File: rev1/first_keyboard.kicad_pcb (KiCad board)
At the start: 2 copper layers, 80 parts, among them SW1 SW_Push, SW10 SW_Push, SW11 SW_Push, SW12 SW_Push, SW13 SW_Push, SW14 SW_Push, SW15 SW_Push, SW16 SW_Push, SW17 SW_Push, SW18 SW_Push, SW19 SW_Push, SW2 SW_Push, SW20 SW_Push, SW21 SW_Push, SW22 SW_Push, SW23 SW_Push, SW24 SW_Push, SW25 SW_Push, SW26 SW_Push, SW27 SW_Push, SW28 SW_Push, SW29 SW_Push, SW3 SW_Push, SW30 SW_Push, SW31 SW_Push, SW32 SW_Push, SW33 SW_Push, SW34 SW_Push, SW35 SW_Push, SW36 SW_Push, SW37 SW_Push, SW38 SW_Push, SW39 SW_Push, SW4 SW_Push, SW40 SW_Push, SW5 SW_Push, SW6 SW_Push, SW7 SW_Push, SW8 SW_Push, SW9 SW_Push, U1 Pico

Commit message: feat:ダイオードの番号降り直しと整列\
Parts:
- SW1: footprint kbd_Parts:ResetSW -> kbd_SW:CherryMX_Hotswap_1u
- SW39: footprint kbd_SW:CherryMX_Hotswap_1u -> kbd_SW:CherryMX_Hotswap_2u
- SW40: footprint kbd_SW:CherryMX_Hotswap_2u -> kbd_Parts:ResetSW
- moved SW1 312.8 mm to (23.8, 45.2)
- moved U1 178.0 mm to (147.7, 61.9)
- moved SW9 134.8 mm to (61.9, 45.2)
- moved SW17 119.1 mm to (100.0, 45.2)
- moved SW40 118.2 mm to (381.0, 132.5)
- moved SW12 114.4 mm to (176.2, 102.4)
- moved SW16 114.4 mm to (195.3, 102.4)
- moved SW5 91.5 mm to (42.9, 45.2)
- moved SW13 81.0 mm to (81.0, 45.2)
- moved SW23 77.5 mm to (176.2, 45.2)
- moved SW4 76.3 mm to (100.0, 102.4)
- moved SW8 76.3 mm to (119.1, 102.4)
- moved SW20 55.7 mm to (119.1, 45.2)
- moved SW29 55.7 mm to (214.3, 45.2)
- moved SW32 55.7 mm to (233.4, 45.2)
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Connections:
- SW1 pad 1: reset -> Col0
- SW1 pad 2: GND -> Net-(D1-A)
- SW10 pad 2: Net-(D9-A) -> Net-(D10-A)
- SW11 pad 2: Net-(D10-A) -> Net-(D11-A)
- SW12 pad 2: Net-(D11-A) -> Net-(D12-A)
- SW13 pad 1: Col2 -> Col3
- SW13 pad 2: Net-(D12-A) -> Net-(D13-A)
- SW14 pad 2: Net-(D13-A) -> Net-(D14-A)
- SW15 pad 2: Net-(D14-A) -> Net-(D15-A)
- SW16 pad 2: Net-(D15-A) -> Net-(D16-A)
- SW17 pad 1: Col3 -> Col4
- SW17 pad 2: Net-(D16-A) -> Net-(D17-A)
- SW18 pad 2: Net-(D17-A) -> Net-(D18-A)
- SW19 pad 2: Net-(D18-A) -> Net-(D19-A)
- SW2 pad 2: Net-(D1-A) -> Net-(D2-A)
- SW20 pad 1: Col4 -> Col5
- SW20 pad 2: Net-(D19-A) -> Net-(D20-A)
- SW21 pad 2: Net-(D20-A) -> Net-(D21-A)
- SW22 pad 2: Net-(D21-A) -> Net-(D22-A)
- SW23 pad 1: Col5 -> Col6
- SW23 pad 2: Net-(D22-A) -> Net-(D23-A)
- SW24 pad 2: Net-(D23-A) -> Net-(D24-A)
- SW25 pad 2: Net-(D24-A) -> Net-(D25-A)
- SW26 pad 1: Col6 -> Col7
- SW26 pad 2: Net-(D25-A) -> Net-(D26-A)
- SW27 pad 2: Net-(D26-A) -> Net-(D27-A)
- SW28 pad 2: Net-(D27-A) -> Net-(D28-A)
- SW29 pad 1: Col7 -> Col8
- SW29 pad 2: Net-(D28-A) -> Net-(D29-A)
- SW3 pad 2: Net-(D2-A) -> Net-(D3-A)
- SW30 pad 2: Net-(D29-A) -> Net-(D30-A)
- SW31 pad 2: Net-(D30-A) -> Net-(D31-A)
- SW32 pad 1: Col8 -> Col9
- SW32 pad 2: Net-(D31-A) -> Net-(D32-A)
- SW33 pad 2: Net-(D32-A) -> Net-(D33-A)
- SW34 pad 2: Net-(D33-A) -> Net-(D34-A)
- SW35 pad 1: Col9 -> Col10
- SW35 pad 2: Net-(D34-A) -> Net-(D35-A)
- SW36 pad 2: Net-(D35-A) -> Net-(D36-A)
- SW37 pad 2: Net-(D36-A) -> Net-(D37-A)
- SW38 pad 1: Col10 -> Col11
- SW38 pad 2: Net-(D37-A) -> Net-(D38-A)
- SW39 pad 2: Net-(D38-A) -> Net-(D39-A)
- SW4 pad 2: Net-(D3-A) -> Net-(D4-A)
- SW40 pad 1: Col11 -> reset
- SW40 pad 2: Net-(D39-A) -> GND
- SW5 pad 1: Col0 -> Col1
- SW5 pad 2: Net-(D4-A) -> Net-(D5-A)
- SW6 pad 2: Net-(D5-A) -> Net-(D6-A)
- SW7 pad 2: Net-(D6-A) -> Net-(D7-A)
- SW8 pad 2: Net-(D7-A) -> Net-(D8-A)
- SW9 pad 1: Col1 -> Col2
- SW9 pad 2: Net-(D8-A) -> Net-(D9-A)

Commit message: feat: すべて整列済み\
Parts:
- moved D1 291.8 mm to (33.3, 51.0), turned to 90 degrees
- moved D2 288.8 mm to (33.3, 70.0), turned to 90 degrees
- moved D3 286.8 mm to (33.3, 89.1), turned to 90 degrees
- moved D5 275.8 mm to (52.4, 51.0), turned to 90 degrees
- moved D6 272.0 mm to (52.4, 70.0), turned to 90 degrees
- moved D7 269.1 mm to (52.4, 89.1), turned to 90 degrees
- moved D9 260.6 mm to (71.4, 51.0), turned to 90 degrees
- moved D10 255.9 mm to (71.4, 70.0), turned to 90 degrees
- moved D11 252.2 mm to (71.4, 89.1), turned to 90 degrees
- moved D13 246.4 mm to (90.5, 51.0), turned to 90 degrees
- moved D14 240.7 mm to (90.5, 70.0), turned to 90 degrees
- moved D15 239.3 mm to (90.5, 89.1), turned to 90 degrees
- moved SW40 235.0 mm to (147.6, 104.8), turned to 180 degrees
- moved D17 229.0 mm to (109.5, 51.0), turned to 90 degrees
- moved D18 224.8 mm to (109.5, 70.0), turned to 90 degrees
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
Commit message: feat: ダイオードそろえた
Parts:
- moved D8 76.8 mm to (52.4, 98.2)
- moved D20 70.6 mm to (76.2, 98.2)
- moved D4 67.4 mm to (42.9, 98.2)
- moved D17 62.2 mm to (69.1, 98.2)
- moved D23 59.3 mm to (221.5, 98.2)
- moved D21 57.4 mm to (78.6, 98.2)
- moved D13 54.0 mm to (64.3, 98.2)
- moved D26 52.9 mm to (228.6, 98.2)
- moved D38 52.9 mm to (257.2, 98.2)
- moved D9 50.1 mm to (54.8, 98.2)
- moved D29 48.8 mm to (235.7, 98.2)
- moved D35 48.8 mm to (250.0, 98.2)
- moved D22 48.5 mm to (81.0, 98.2)
- moved D5 47.8 mm to (45.2, 98.2)
- moved D18 47.4 mm to (71.4, 98.2)
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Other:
- board outline added: 271.5 x 85.7 mm

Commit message: feat: m3spacer
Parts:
- added Ref**: Val**, kbd_Hole:m3_Spacer_Hole, F.Cu at (274.3, 32.0)
- added Ref**: Val**, kbd_Hole:m3_Spacer_Hole, F.Cu at (159.7, 111.5)
- added Ref**: Val**, kbd_Hole:m3_Spacer_Hole, F.Cu at (274.3, 97.0)
- added Ref**: Val**, kbd_Hole:m3_Spacer_Hole, F.Cu at (135.6, 111.5)
- added Ref**: Val**, kbd_Hole:m3_Spacer_Hole, F.Cu at (120.7, 32.0)
- added Ref**: Val**, kbd_Hole:m3_Spacer_Hole, F.Cu at (171.4, 32.0)
- added Ref**: Val**, kbd_Hole:m3_Spacer_Hole, F.Cu at (20.3, 97.0)
- added Ref**: Val**, kbd_Hole:m3_Spacer_Hole, F.Cu at (20.3, 32.0)
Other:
- board size 271.5 x 85.7 mm -> 271.5 x 88.6 mm

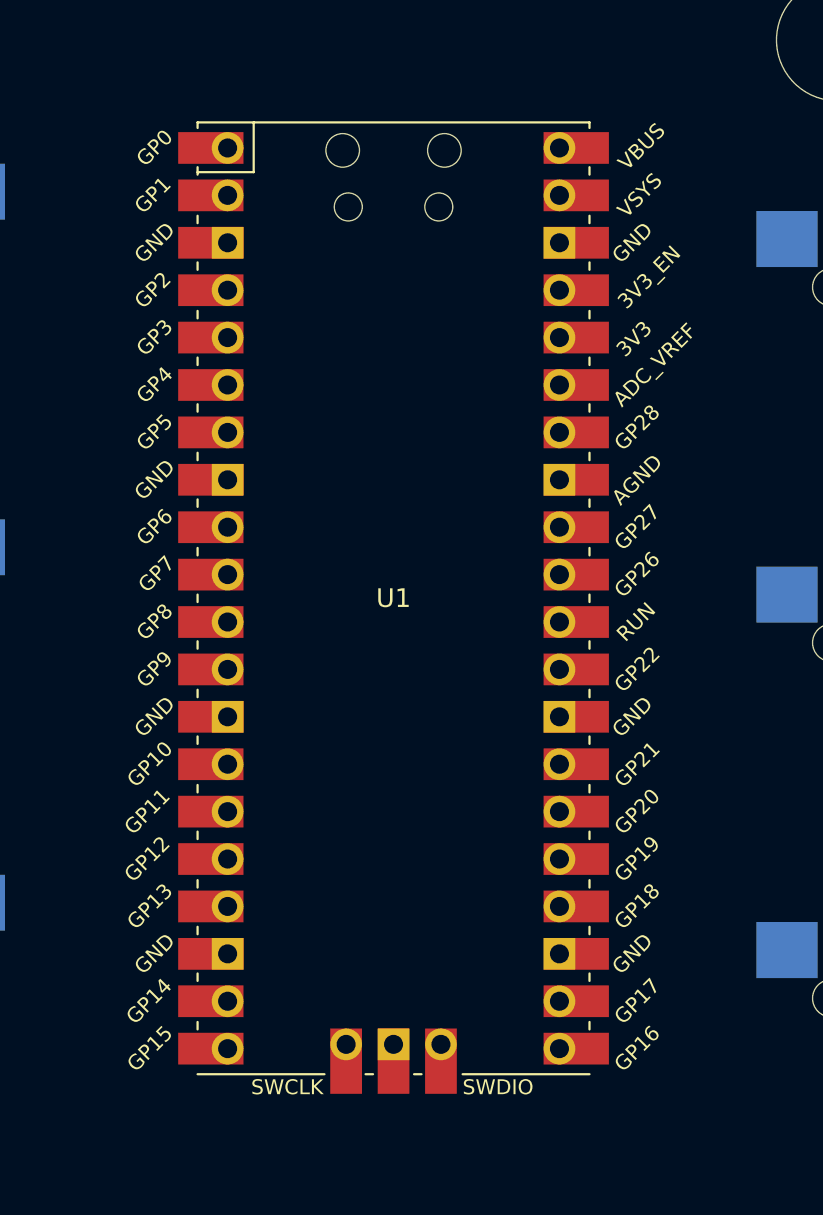
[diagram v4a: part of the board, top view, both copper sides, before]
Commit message: feat: picoを裏面に
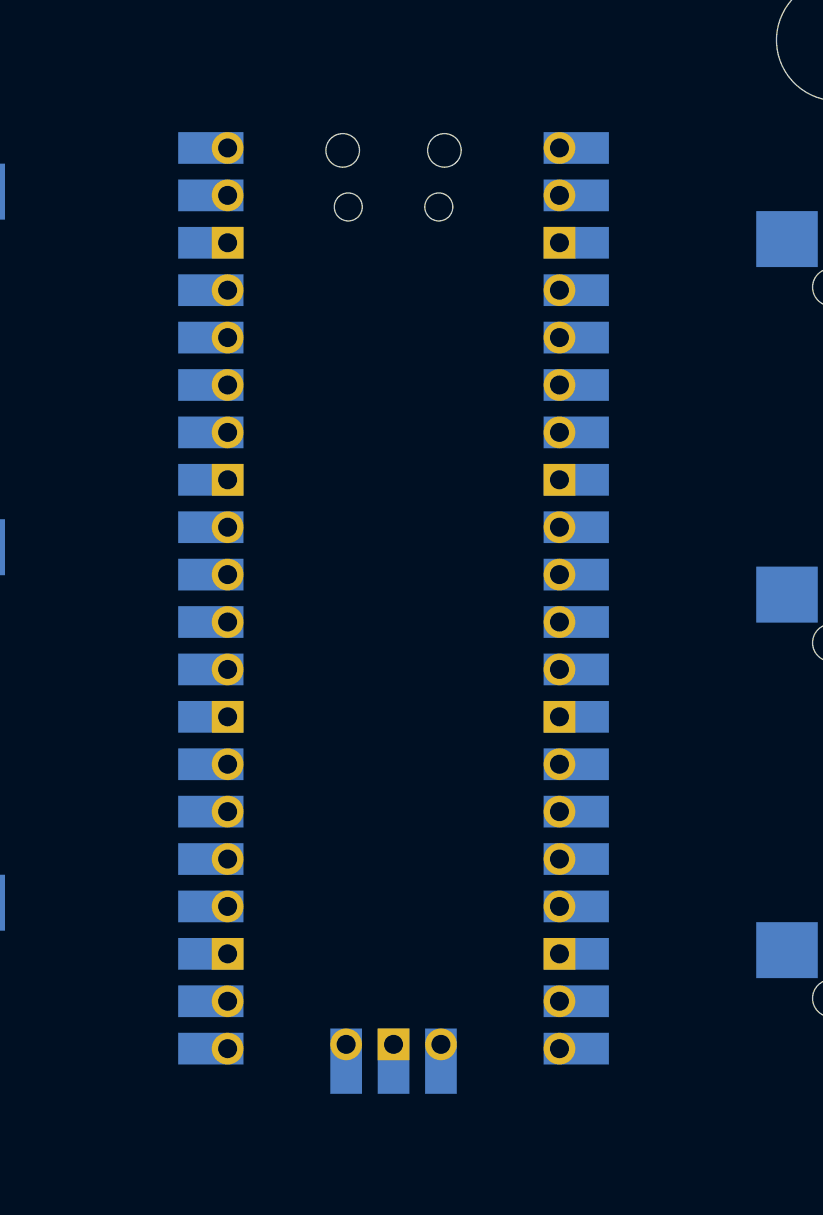
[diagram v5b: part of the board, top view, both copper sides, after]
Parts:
- U1: moved to B.Cu
- turned U1 to 180 degrees

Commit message: feat: ダイオードをスイッチの近くに大移動
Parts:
- Ref1: renamed from Ref**; value Val** -> Val1
- Ref2: renamed from Ref**; value Val** -> Val2
- Ref3: renamed from Ref**; value Val** -> Val3
- Ref4: renamed from Ref**; value Val** -> Val4
- Ref5: renamed from Ref**; value Val** -> Val5
- Ref6: renamed from Ref**; value Val** -> Val6
- Ref7: renamed from Ref**; value Val** -> Val7
- Ref8: renamed from Ref**; value Val** -> Val8
- SW1, SW10, SW11, SW12, SW13, SW14, SW15, SW16, SW17, SW18, SW19, SW2, SW20, SW21, SW22, SW23, SW24, SW25, SW26, SW27, SW28, SW29, SW3, SW30, SW31, SW32, SW33, SW34, SW35, SW36, SW37, SW38, SW4, SW5, SW6, SW7, SW8, SW9: footprint kbd_SW:CherryMX_Hotswap_1u -> kbd_SW:CherryMX_Solder_1u
- SW39: footprint kbd_SW:CherryMX_Hotswap_2u -> kbd_SW:CherryMX_Solder_2u
- U1: moved to F.Cu
- moved D23 77.9 mm to (166.7, 42.9)
- moved D26 70.0 mm to (185.7, 42.9)
- moved D24 67.7 mm to (166.7, 61.9)
- moved D20 64.6 mm to (109.5, 42.9)
- moved D29 63.4 mm to (204.8, 42.9)
- moved D25 62.0 mm to (166.7, 81.0)
- moved D1 59.4 mm to (14.3, 42.9)
- moved D17 59.4 mm to (90.5, 42.9)
- moved D32 58.6 mm to (223.8, 42.9)
- moved D27 58.0 mm to (185.7, 61.9)
- moved D8 57.2 mm to (109.5, 100.6)
- moved D5 56.6 mm to (33.3, 42.9)
- moved D13 55.8 mm to (71.4, 42.9)
- moved D35 55.8 mm to (242.9, 42.9)
- moved D38 55.6 mm to (261.9, 42.9)
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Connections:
- SW12 pad 1: Col2 -> Col6
- SW16 pad 1: Col3 -> Col7
- SW4 pad 1: Col0 -> Col4
- SW8 pad 1: Col1 -> Col5
- U1 pad 10: Row1 -> Row2
- U1 pad 11: Row2 -> Row1
- U1 pad 12: Row3 -> Row0
- U1 pad 26: unconnected-(U1-GPIO20-Pad26) -> Col10
- U1 pad 27: unconnected-(U1-GPIO21-Pad27) -> Col11
- U1 pad 38: GND -> unconnected-(U1-GND-Pad38)
- U1 pad 9: Row0 -> Row3
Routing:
- net Row0: track 0.00 -> 306.0 mm
- net Row2: track 0.00 -> 293.9 mm, vias 0 -> 1
- net Row1: track 0.00 -> 286.7 mm
- net Col0: track 0.00 -> 157.0 mm
- net Row3: track 0.00 -> 154.0 mm
- net Col11: track 0.00 -> 147.4 mm
- net Col10: track 0.00 -> 142.2 mm
- net Col1: track 0.00 -> 141.4 mm
- net Col2: track 0.00 -> 131.0 mm
- net GND: track 0.00 -> 118.7 mm
- net Col9: track 0.00 -> 113.7 mm
- net Col3: track 0.00 -> 102.7 mm
- net Col4: track 0.00 -> 102.6 mm
- net Col7: track 0.00 -> 94.9 mm
- net Col8: track 0.00 -> 93.6 mm
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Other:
- board text added: "madbd v0.0.1 Design by @amkkr X: @ama_O255"

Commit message: fix: ねじ穴に変更
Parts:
- Ref1, Ref2, Ref3, Ref4, Ref5, Ref6, Ref7, Ref8: footprint kbd_Hole:m3_Spacer_Hole -> MountingHole:MountingHole_3.2mm_M3
- SW1, SW10, SW11, SW12, SW13, SW14, SW15, SW16, SW17, SW18, SW19, SW2, SW20, SW21, SW22, SW23, SW24, SW25, SW26, SW27, SW28, SW29, SW3, SW30, SW31, SW32, SW33, SW34, SW35, SW36, SW37, SW38, SW4, SW5, SW6, SW7, SW8, SW9: footprint kbd_SW:CherryMX_Solder_1u -> kbd_SW:CherryMX_Hotswap_1u
- SW39: footprint kbd_SW:CherryMX_Solder_2u -> kbd_SW:CherryMX_Hotswap_2u
- moved U1 7.14 mm to (147.6, 54.8)
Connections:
- U1 pad 10: Row2 -> Col10
- U1 pad 11: Row1 -> Col9
- U1 pad 12: Row0 -> Col8
- U1 pad 14: Col0 -> Col7
- U1 pad 15: Col1 -> Col6
- U1 pad 16: Col2 -> Col5
- U1 pad 17: Col3 -> Col4
- U1 pad 19: Col4 -> Col3
- U1 pad 20: Col5 -> Col2
- U1 pad 21: Col6 -> Col1
- U1 pad 22: Col7 -> Col0
- U1 pad 24: Col8 -> Row3
- U1 pad 25: Col9 -> Row2
- U1 pad 26: Col10 -> Row1
- U1 pad 27: Col11 -> Row0
- U1 pad 9: Row3 -> Col11
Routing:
- net Row0: track 306.0 -> 0.00 mm
- net Row2: track 293.9 -> 0.00 mm, vias 1 -> 0
- net Row1: track 286.7 -> 0.00 mm
- net Col0: track 157.0 -> 0.00 mm
- net Row3: track 154.0 -> 0.00 mm
- net Col11: track 147.4 -> 0.00 mm
- net Col10: track 142.2 -> 0.00 mm
- net Col1: track 141.4 -> 0.00 mm
- net Col2: track 131.0 -> 0.00 mm
- net GND: track 118.7 -> 0.00 mm
- net Col9: track 113.7 -> 0.00 mm
- net Col3: track 102.7 -> 0.00 mm
- net Col4: track 102.6 -> 0.00 mm
- net Col7: track 94.9 -> 0.00 mm
- net Col8: track 93.6 -> 0.00 mm
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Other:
- board outline removed

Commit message: feat: 回路図にスイッチを追加
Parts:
- U1: moved to B.Cu
- moved Ref3 16.2 mm to (187.6, 32.0)
- moved SW16 16.2 mm to (211.5, 102.4)
- moved SW26 16.2 mm to (211.5, 45.2)
- moved SW27 16.2 mm to (211.5, 64.3)
- moved SW28 16.2 mm to (211.5, 83.3)
- moved SW35 16.2 mm to (268.6, 45.2)
- moved SW36 16.2 mm to (268.6, 64.3)
- moved SW37 16.2 mm to (268.6, 83.3)
- moved D12 16.2 mm to (182.9, 100.6)
- moved D16 16.2 mm to (201.9, 100.0)
- moved D23 16.2 mm to (182.9, 42.9)
- moved D24 16.2 mm to (182.9, 61.9)
- moved D25 16.2 mm to (182.9, 81.0)
- moved D26 16.2 mm to (201.9, 42.9)
- moved D27 16.2 mm to (201.9, 61.9)
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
